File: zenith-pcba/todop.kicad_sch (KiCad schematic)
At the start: 4 parts, among them U1 XC7A50T-CSG325, U5 TXS0101DB, U6 TXS0101DB

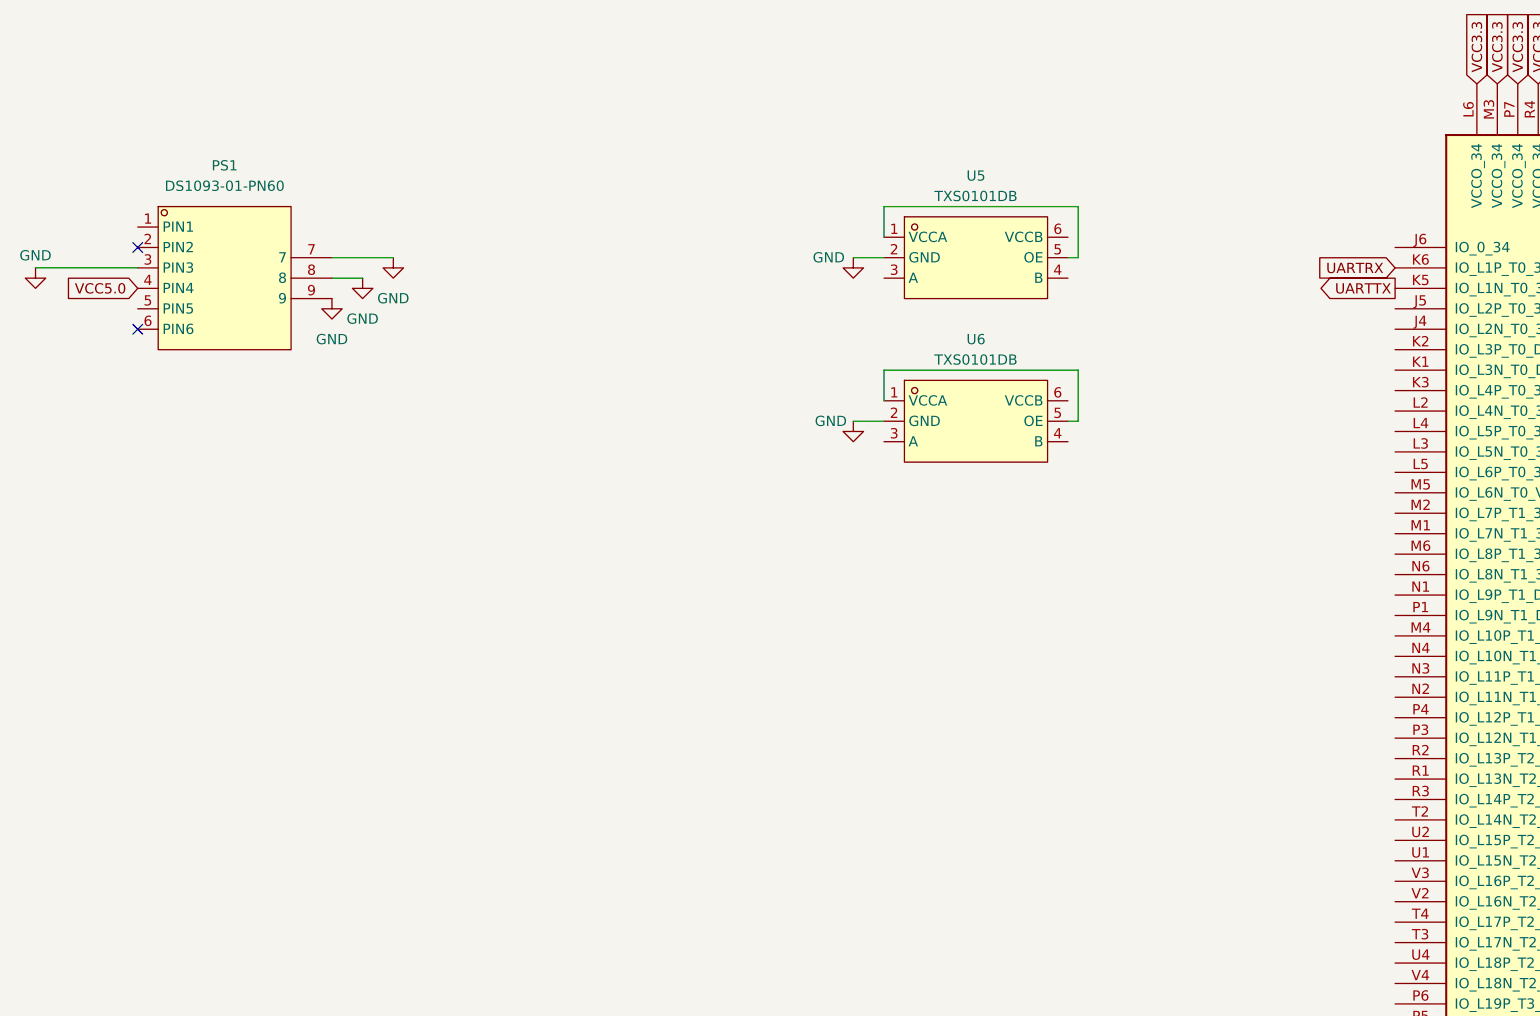
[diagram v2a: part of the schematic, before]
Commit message: feat(pcba): din esd
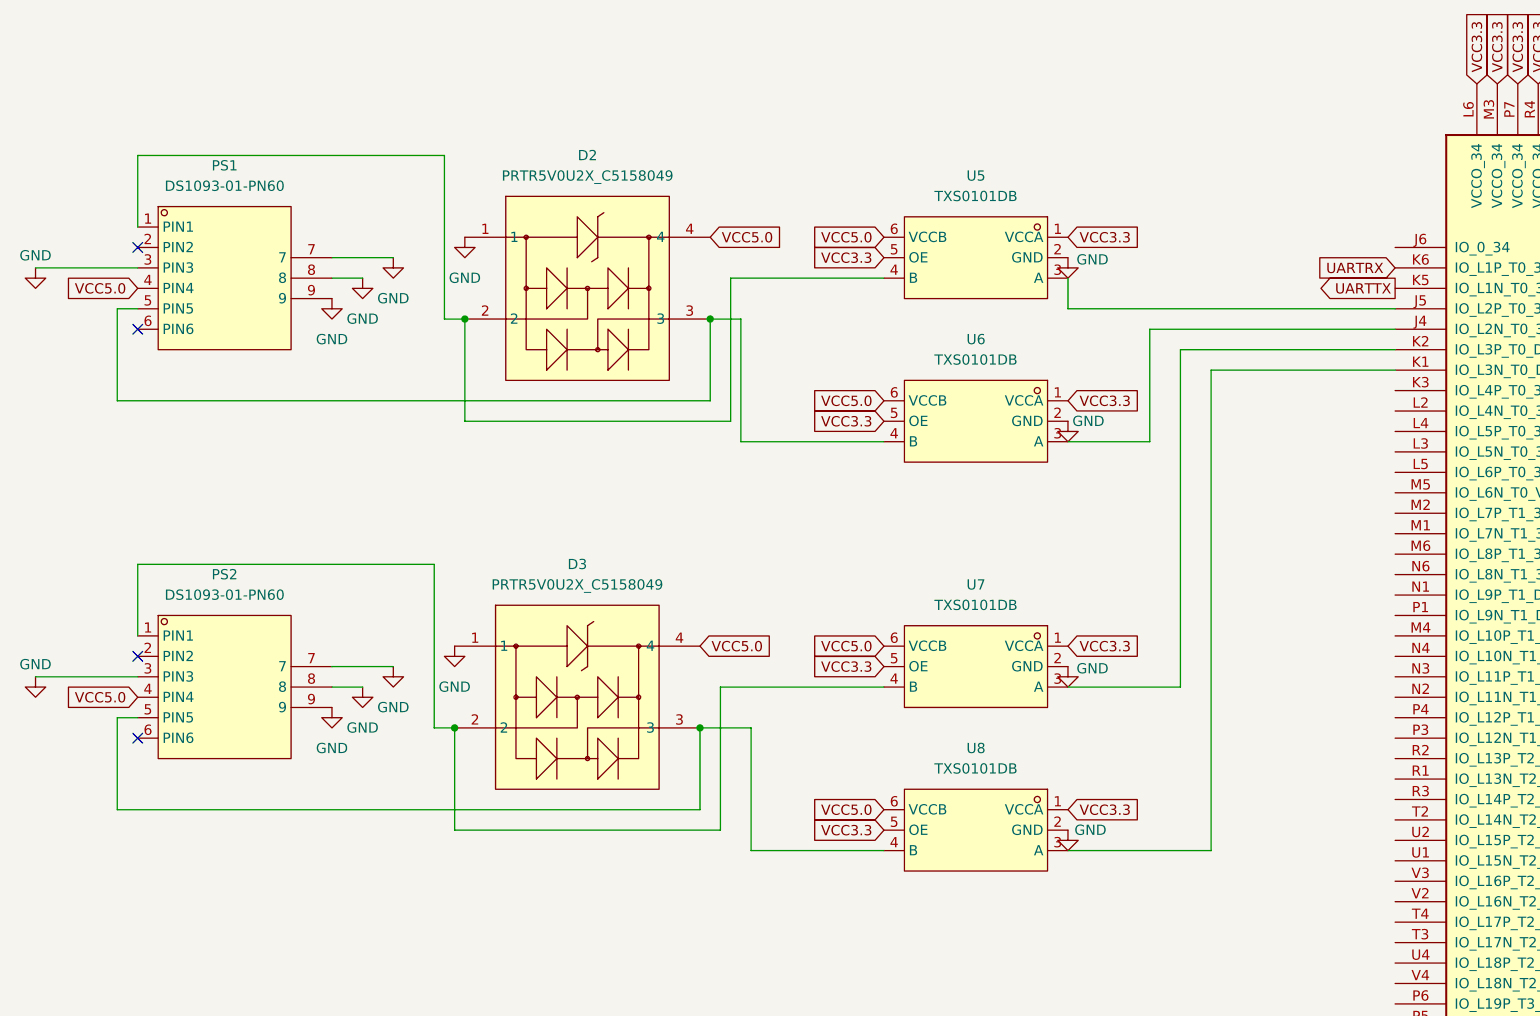
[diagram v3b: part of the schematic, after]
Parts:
- added D2, D3: PRTR5V0U2X_C5158049, easyeda2kicad:SOT-143_L2.9-W1.3-P1.92-LS2.3-BL, symbol easyeda2kicad:PRTR5V0U2X_C5158049
- added PS2: DS1093-01-PN60, easyeda2kicad:CONN-TH_DS1093-01-PN60, symbol easyeda2kicad:DS1093-01-PN60
- added U7, U8: TXS0101DB, easyeda2kicad:SOT-23-6_L2.9-W1.6-P0.95-LS2.9-BL, symbol easyeda2kicad:TXS0101DB
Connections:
- net GND: now also D2.1, D3.1, PS2.3 (PIN3), PS2.7, PS2.8, PS2.9, U7.2 (GND), U8.2 (GND)
- net VCC3.3: now also U5.1 (VCCA), U5.5 (OE), U6.1 (VCCA), U6.5 (OE), U7.1 (VCCA), U7.5 (OE), U8.1 (VCCA), U8.5 (OE)
- net VCC5.0: now also U5.6 (VCCB), U6.6 (VCCB), D2.4, D3.4, PS2.4 (PIN4), U7.6 (VCCB), U8.6 (VCCB)
- net at U1.J4 (IO_L2N_T0_34): now also U6.3 (A)
- net at U1.J5 (IO_L2P_T0_34): now also U5.3 (A)
- net at U1.K1 (IO_L3N_T0_DQS_34): now also U8.3 (A)
- net at U1.K2 (IO_L3P_T0_DQS_34): now also U7.3 (A)
- net at PS1.1 (PIN1): now also U5.4 (B), D2.2
- net at PS1.5 (PIN5): now also U6.4 (B), D2.3
- new net: D3.2, PS2.1 (PIN1), U7.4 (B)
- new net: D3.3, PS2.5 (PIN5), U8.4 (B)
- no-connect marks 2 -> 4

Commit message: feat(pcba): sd card schematic
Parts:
- removed unit 4 of U1
- removed unit 3 of U1
- added C10: CC0603MRX5R7BB106, easyeda2kicad:C0603, symbol easyeda2kicad:CC0603MRX5R7BB106
- added C8, C9: CL10B104KA8NNNC, easyeda2kicad:C0603, symbol easyeda2kicad:CL10B104KA8NNNC
- added Card1: 5025700893, easyeda2kicad:TF-SMD_5025700893, symbol easyeda2kicad:5025700893
- added D4: TPD6E004RSER, easyeda2kicad:UQFN-8_L1.5-W1.5-P0.50-TL, symbol easyeda2kicad:TPD6E004RSER
- added R10, R11, R12, R13, R14, R15: RC0402FR-0722R1L, easyeda2kicad:R0402, symbol easyeda2kicad:RC0402FR-0722R1L
- added R16, R5, R6, R7, R8, R9: RC0402FR-0710KL, easyeda2kicad:R0402, symbol easyeda2kicad:RC0402FR-0710KL
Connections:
- net GND: now also C10.1, C8.2, C9.1, Card1.11 (VSS), Card1.6 (VSS), Card1.9 (EH), D4.4 (GND)
- net VCC3.3: now also C10.2, C9.2, Card1.4 (VDD), D4.8 (VCC), R16.1, R5.1, R6.1, R7.1, R8.1, R9.1
- net at U1.K3 (IO_L4P_T0_34): now also R10.2
- net at U1.L2 (IO_L4N_T0_34): now also R11.2
- net at U1.L3 (IO_L5N_T0_34): now also R13.2
- net at U1.L4 (IO_L5P_T0_34): now also R12.2
- net at U1.L5 (IO_L6P_T0_34): now also R14.2
- net SDSW: now reaches U1.M2 (IO_L7P_T1_34)
- net SDSW: now also C8.1, Card1.10 (DET-SW), R16.2
- net at U1.M5 (IO_L6N_T0_VREF_34): now also R15.2
- new net SDCLK: Card1.5 (CLK), D4.6 (IO5), R15.1
- new net SDCMD: Card1.3 (CMD), D4.5 (IO4), R14.1, R7.2
- new net SDDAT0: Card1.7 (DAT0), D4.1 (IO1), R10.1, R8.2
- new net SDDAT1: Card1.8 (DAT1), D4.2 (IO2), R11.1, R9.2
- new net SDDAT2: Card1.1 (DAT2), D4.3 (IO3), R12.1, R5.2
- new net SDDAT3: Card1.2 (CD/DAT3), D4.7 (IO6), R13.1, R6.2

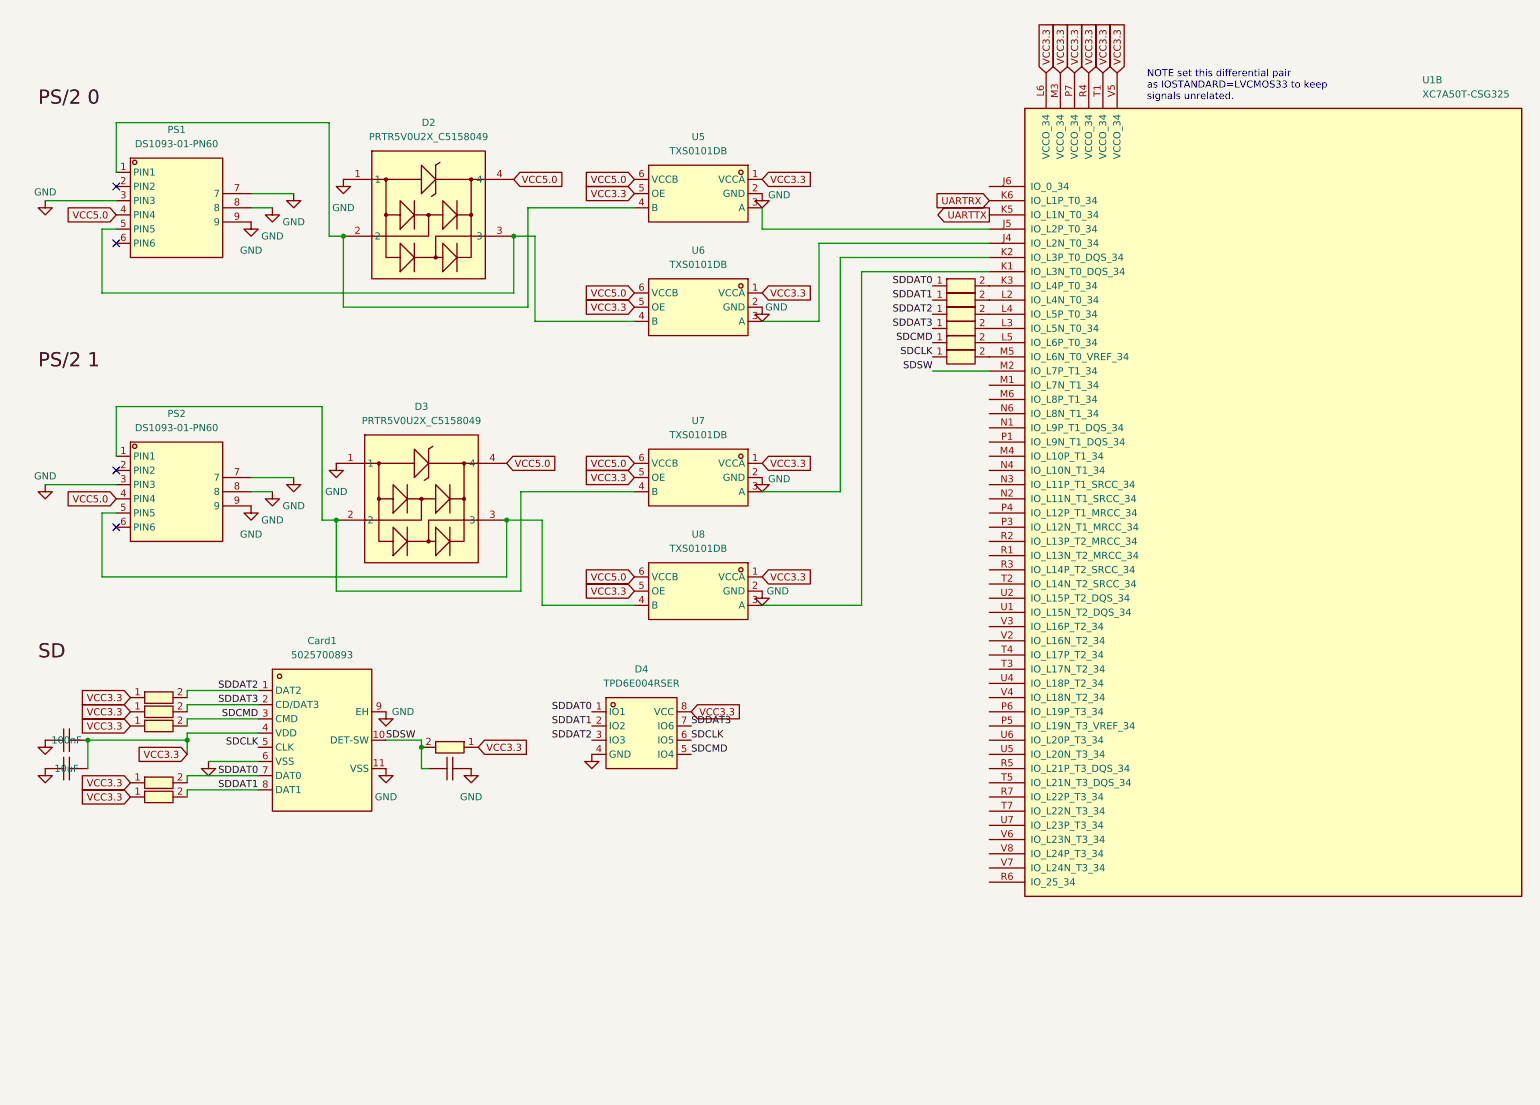
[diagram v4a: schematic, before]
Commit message: feat(pcba): migrate to kintex fpga
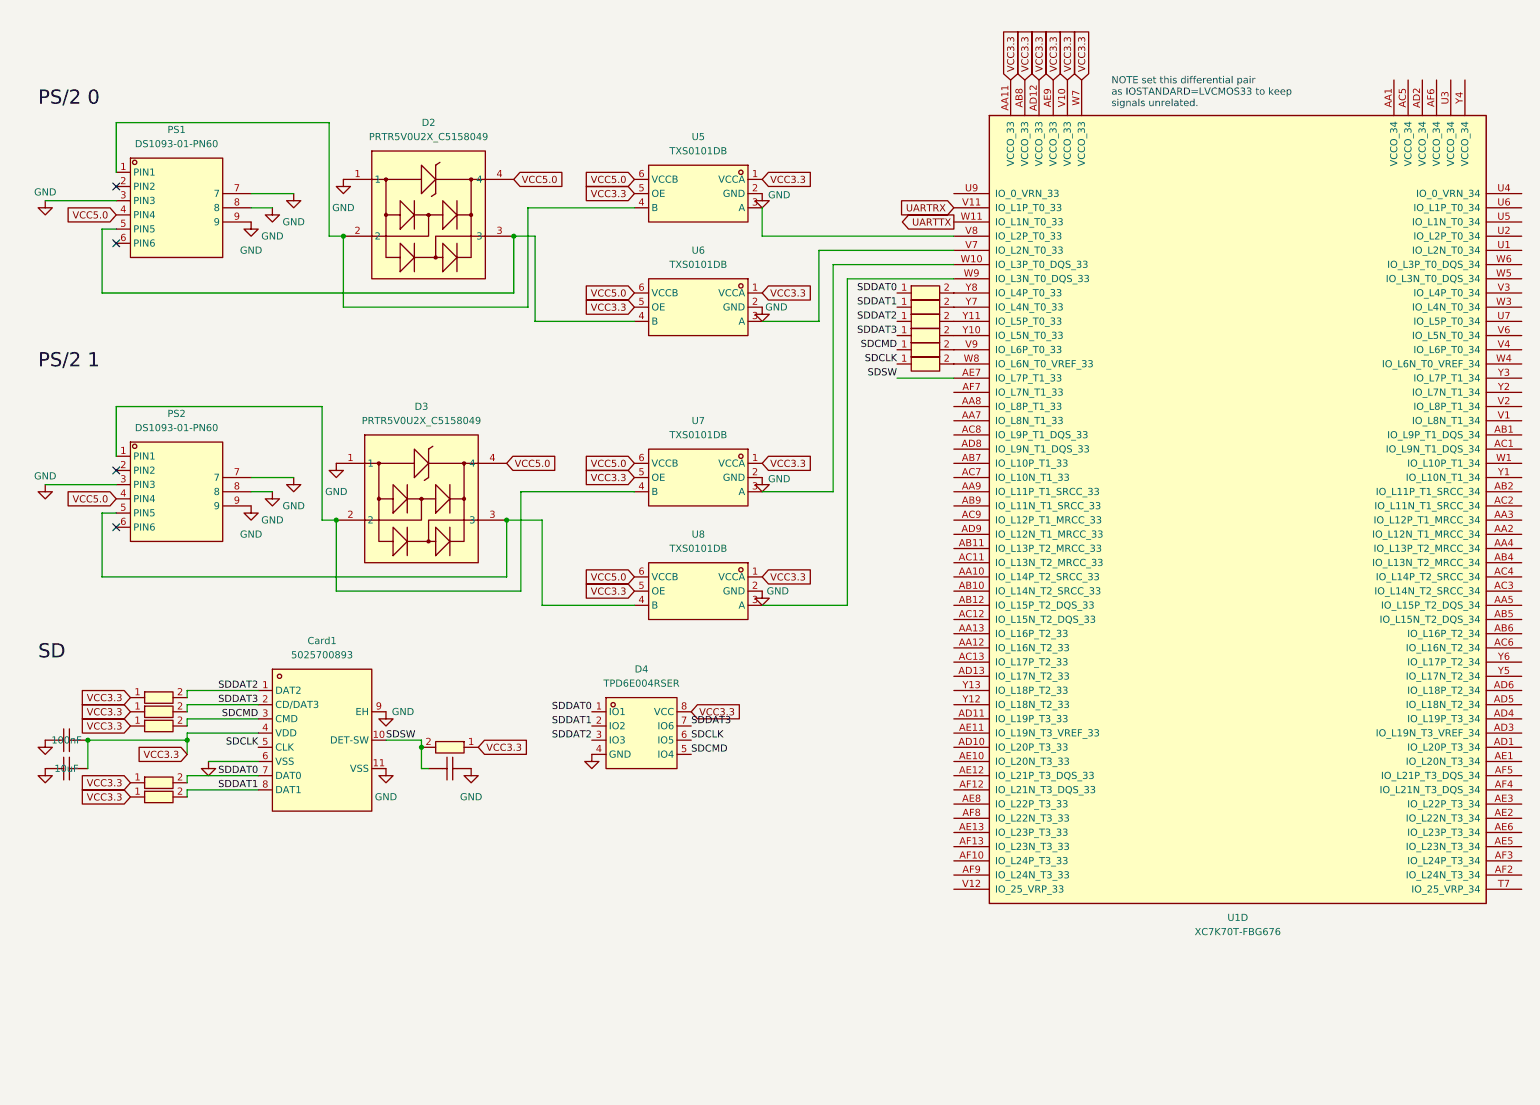
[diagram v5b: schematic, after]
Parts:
- removed U1: XC7A50T-CSG325, Package_BGA:Xilinx_CSG325, symbol FPGA_Xilinx_Artix7:XC7A50T-CSG325
- added U1: XC7K70T-FBG676, easyeda2kicad:FBGA-676_L27.0-W27.0-R26-C26-P1.00-BL, symbol FPGA_Xilinx_Kintex7:XC7K70T-FBG676
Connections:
- net SDSW: now also U1.AE7 (IO_L7P_T1_33)
- net UARTRX: now also U1.V11 (IO_L1P_T0_33)
- net UARTTX: now also U1.W11 (IO_L1N_T0_33)
- net VCC3.3: now also U1.AA11 (VCCO_33), U1.AB8 (VCCO_33), U1.AD12 (VCCO_33), U1.AE9 (VCCO_33), U1.V10 (VCCO_33), U1.W7 (VCCO_33)
- net at U8.3 (A): now also U1.W9 (IO_L3N_T0_DQS_33)
- net at R15.2: now also U1.W8 (IO_L6N_T0_VREF_33)
- net at R14.2: now also U1.V9 (IO_L6P_T0_33)
- net at R11.2: now also U1.Y7 (IO_L4N_T0_33)
- net at U6.3 (A): now also U1.V7 (IO_L2N_T0_33)
- net at U5.3 (A): now also U1.V8 (IO_L2P_T0_33)
- net at U7.3 (A): now also U1.W10 (IO_L3P_T0_DQS_33)
- net at R10.2: now also U1.Y8 (IO_L4P_T0_33)
- net at R13.2: now also U1.Y10 (IO_L5N_T0_33)
- net at R12.2: now also U1.Y11 (IO_L5P_T0_33)

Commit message: feat(pcba): pcb edge cuts
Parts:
- added DSub1: DS1038-15FBNSIA74-0CC, easyeda2kicad:DSUB-TH_DS1038-15FBNSIA74-0CC, symbol easyeda2kicad:DS1038-15FBNSIA74-0CC
- added R17: RC0402JR-07510RL, easyeda2kicad:R0402, symbol easyeda2kicad:RC0402JR-07510RL
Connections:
- net GND: now also DSub1.10, DSub1.16, DSub1.17, DSub1.5, DSub1.6, DSub1.7, DSub1.8
- net VSYNC: now reaches U1.AA8 (IO_L8P_T1_33)
- net VSYNC: now also DSub1.14
- net HSYNC: now reaches U1.AF7 (IO_L7N_T1_33)
- net HSYNC: now also DSub1.13
- no-connect marks 4 -> 9

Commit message: feat(pcba): vga
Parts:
- added R18, R20, R22: RC0402FR-071K02L, easyeda2kicad:R0402, symbol easyeda2kicad:RC0402FR-071K02L
- added R19, R21: RC0402JR-07510RL, easyeda2kicad:R0402, symbol easyeda2kicad:RC0402JR-07510RL
- added R23: RC0402DR-072K05L, easyeda2kicad:R0402, symbol easyeda2kicad:RC0402DR-072K05L
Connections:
- net VGAR1: now reaches U1.AA7 (IO_L8N_T1_33)
- net VGAR1: now also R17.2
- net VGAB1: now reaches U1.AA9 (IO_L11P_T1_SRCC_33)
- net VGAB1: now also R21.2
- net VGAG1: now reaches U1.AB7 (IO_L10P_T1_33)
- net VGAG1: now also R20.2
- net VGAB0: now reaches U1.AB9 (IO_L11N_T1_SRCC_33)
- net VGAB0: now also R22.2
- net VGAG0: now reaches U1.AC7 (IO_L10N_T1_33)
- net VGAG0: now also R23.2
- net VGAR0: now reaches U1.AC8 (IO_L9P_T1_DQS_33)
- net VGAR0: now also R18.2
- net VGAG2: now reaches U1.AD8 (IO_L9N_T1_DQS_33)
- net VGAG2: now also R19.2
- net at DSub1.1: now also R17.1, R18.1
- net at DSub1.2: now also R19.1, R20.1, R23.1
- net at DSub1.3: now also R21.1, R22.1
- net HSYNC renamed VGAHSYNC
- net VSYNC renamed VGAVSYNC

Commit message: feat(pcba): vga level shifter
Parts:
- added D5: TPESD7538P, easyeda2kicad:DFN3810-9_L3.8-W1.0-P0.9, symbol easyeda2kicad:TPESD7538P
- added U10, U9: TXS0101DB, easyeda2kicad:SOT-23-6_L2.9-W1.6-P0.95-LS2.9-BL, symbol easyeda2kicad:TXS0101DB
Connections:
- net GND: now also D5.3, U10.2 (GND), U9.2 (GND)
- net VCC3.3: now also U10.1 (VCCA), U10.5 (OE), U9.1 (VCCA), U9.5 (OE)
- net VCC5.0: now also DSub1.9, U10.6 (VCCB), U9.6 (VCCB)
- net VGAHSYNC: now also D5.5
- net VGAVSYNC: now also D5.6
- net VGASDA: now reaches U1.AC9 (IO_L12P_T1_MRCC_33)
- net VGASDA: now also U9.3 (A)
- net VGASCL: now reaches U1.AD9 (IO_L12N_T1_MRCC_33)
- net VGASCL: now also U10.3 (A)
- net VGAR: now reaches DSub1.1, R17.1, R18.1
- net VGAR: now also D5.1
- net VGAG: now reaches DSub1.2, R19.1, R20.1, R23.1
- net VGAG: now also D5.2
- net VGAB: now reaches DSub1.3, R21.1, R22.1
- net VGAB: now also D5.4
- net VGASDA5: now reaches DSub1.12
- net VGASDA5: now also D5.7, U9.4 (B)
- net VGASCL5: now reaches DSub1.15
- net VGASCL5: now also D5.8, U10.4 (B)
- no-connect marks 9 -> 7
